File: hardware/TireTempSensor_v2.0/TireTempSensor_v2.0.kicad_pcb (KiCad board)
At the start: 4 copper layers, 27 x 53.8 mm, 54 parts, among them IC1 MAX15462AATA+, IC2 MLX90621ESF-BAB-000-SP, J1 SWD_01x06, J2 CAN_01x04, Q1 FQT3P20TF, SW1 RESET, U1 STM32L4P5RET6, U2 MIC5306-2.6YD5-TR, U3 SN65HVD232, Y1 16MGHz

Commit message: some pcb connections
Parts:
- F1: footprint Capacitor_SMD:C_1206_3216Metric -> Fuse:Fuse_1210_3225Metric
- J2: footprint Connector_PinHeader_1.27mm:PinHeader_1x04_P1.27mm_Vertical -> Connector_Wire:SolderWire-0.1sqmm_1x04_P3.6mm_D0.4mm_OD1mm_Relief
- moved FB1 19.8 mm to (119.8, 89.2)
- moved C14 8.33 mm to (124.5, 76.0), turned to -90 degrees
- moved C15 8.08 mm to (118.5, 75.2)
- moved U2 8.08 mm to (121.5, 75.0)
- moved FB2 7.41 mm to (122.8, 78.5), turned to 90 degrees
- moved J2 5.04 mm to (116.9, 115.5), turned to 180 degrees
- moved J1 4.86 mm to (123.5, 82.8)
- moved R6 3.00 mm to (116.8, 69.0)
- moved C17 3.00 mm to (108.8, 69.0)
- moved FB3 3.00 mm to (108.8, 72.2)
- moved R5 3.00 mm to (116.8, 72.2)
- moved IC2 2.95 mm to (114.5, 68.7)
- moved F1 2.69 mm to (114.0, 108.5)
- moved H1 2.00 mm to (122.2, 113.5)
- moved H2 2.00 mm to (103.2, 113.5)
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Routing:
- net GND: track 0.00 -> 15.6 mm
- net /+3V3_uC: track 0.00 -> 13.2 mm
- net +2V6: track 0.00 -> 12.9 mm
- net /OSC IN: track 0.00 -> 10.6 mm
- net Net-(F1-Pad2): track 0.00 -> 10.5 mm
- net Net-(R3-Pad1): track 0.00 -> 8.09 mm
- net /NRST: track 0.00 -> 8.01 mm
- net Net-(C14-Pad1): track 0.00 -> 6.32 mm
- net /CAN L: track 0.00 -> 4.41 mm
- net /CAN H: track 0.00 -> 4.41 mm
- net Net-(C17-Pad1): track 0.00 -> 4.24 mm
- net Net-(C10-Pad1): track 0.00 -> 3.98 mm
- net /Power Supply 3.3v 2.6v/+24V safe: track 0.00 -> 3.75 mm
- net Net-(FB4-Pad2): track 0.00 -> 2.85 mm
- net Net-(D6-Pad2): track 0.00 -> 2.61 mm
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- added copper zone on In1.Cu, net GND
- added copper zone on F.Cu, net Net-(L1-Pad1)
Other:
- board size 27 x 53.8 mm -> 27 x 54 mm

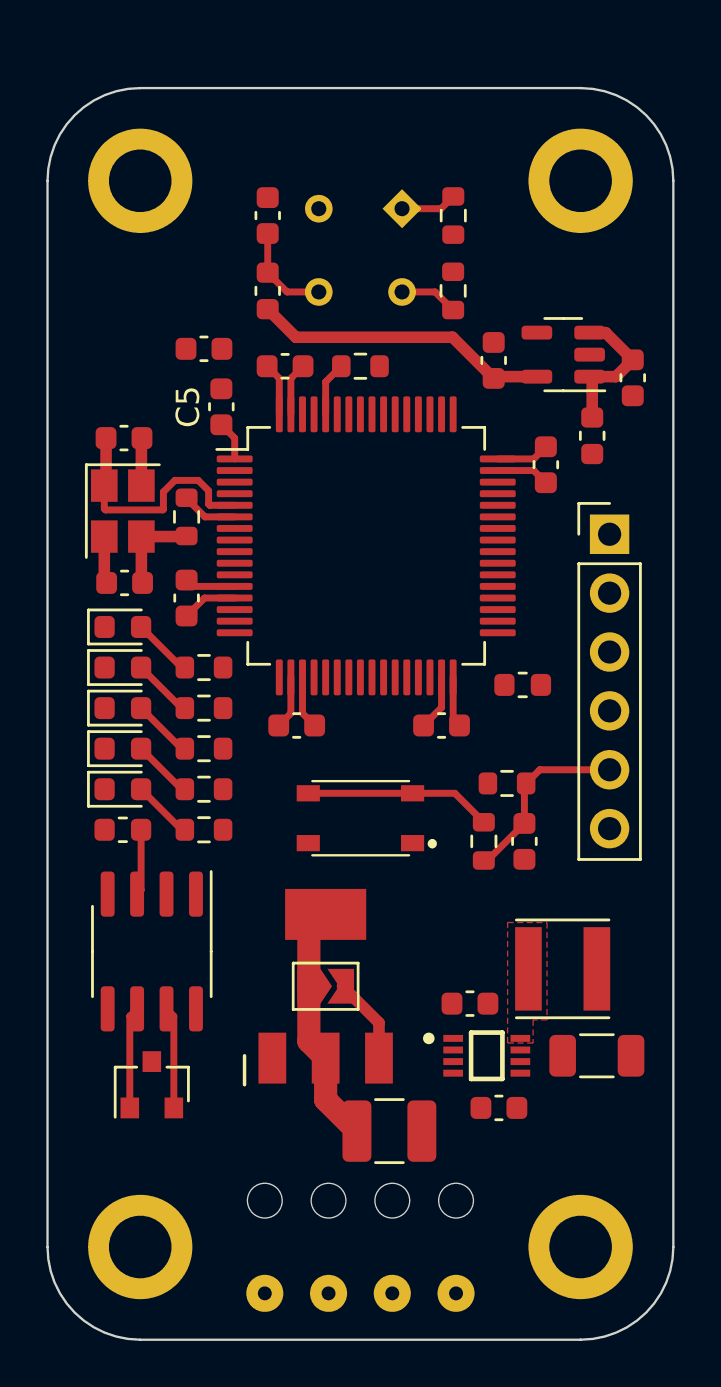
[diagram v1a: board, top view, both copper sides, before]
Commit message: more pcb connections
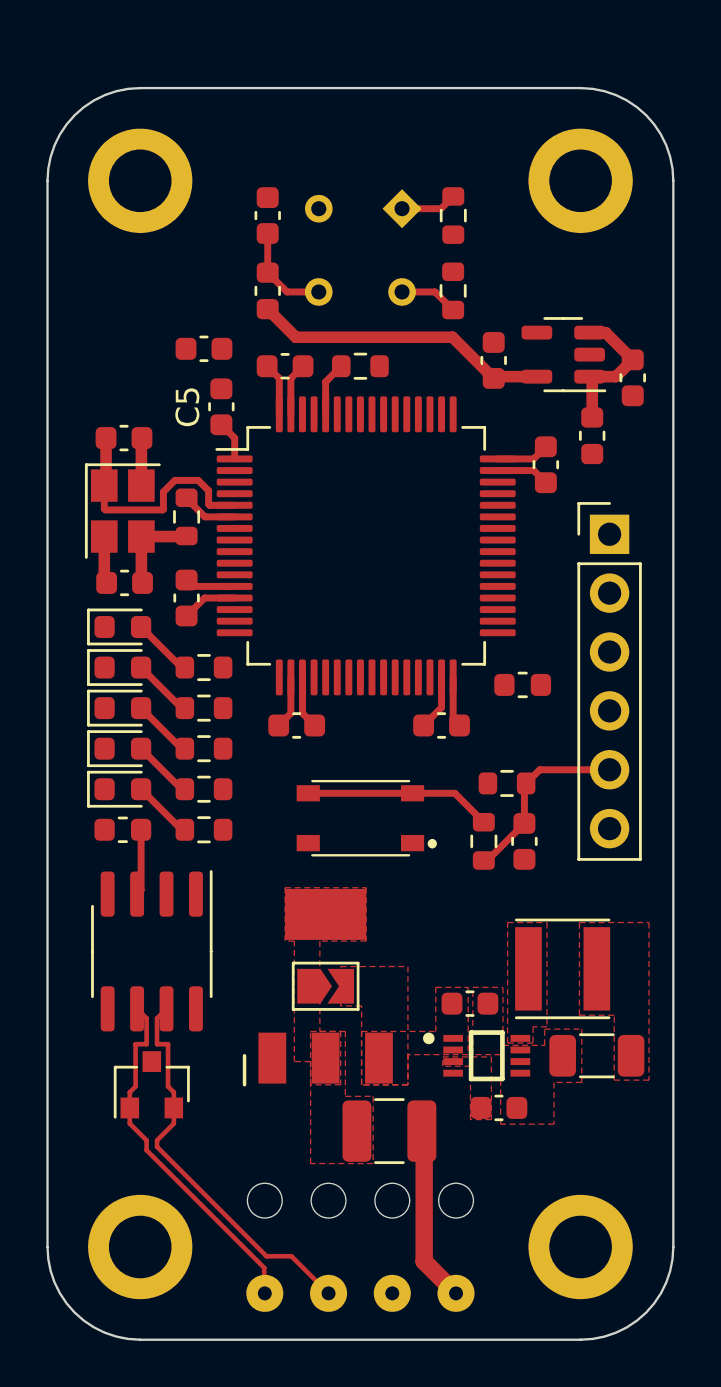
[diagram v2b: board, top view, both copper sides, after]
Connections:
- D1 pad 1: /CAN L -> /CAN -
- D1 pad 2: /CAN H -> /CAN +
- J2 pad 2: /CAN H -> GND
- J2 pad 3: /CAN L -> /CAN +
- J2 pad 4: GND -> /CAN -
- U3 pad 6: /CAN L -> /CAN -
- U3 pad 7: /CAN H -> /CAN +
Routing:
- net /CAN +: track 0.00 -> 17.0 mm
- net /CAN -: track 0.00 -> 15.4 mm
- net Net-(F1-Pad2): track 10.5 -> 0.00 mm
- net +24V: track 0.00 -> 7.61 mm
- net /CAN L: track 4.41 -> 0.00 mm
- net /CAN H: track 4.41 -> 0.00 mm
- net /Power Supply 3.3v 2.6v/+24V safe: track 3.75 -> 0.00 mm
- added copper zone on F.Cu, net +3V3
- added copper zone on F.Cu, net /Power Supply 3.3v 2.6v/+24V safe
- added copper zone on F.Cu, net GND
- added copper zone on F.Cu, net Net-(C13-Pad1)
- added copper zone on F.Cu, net Net-(F1-Pad2)

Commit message: gnd vias added
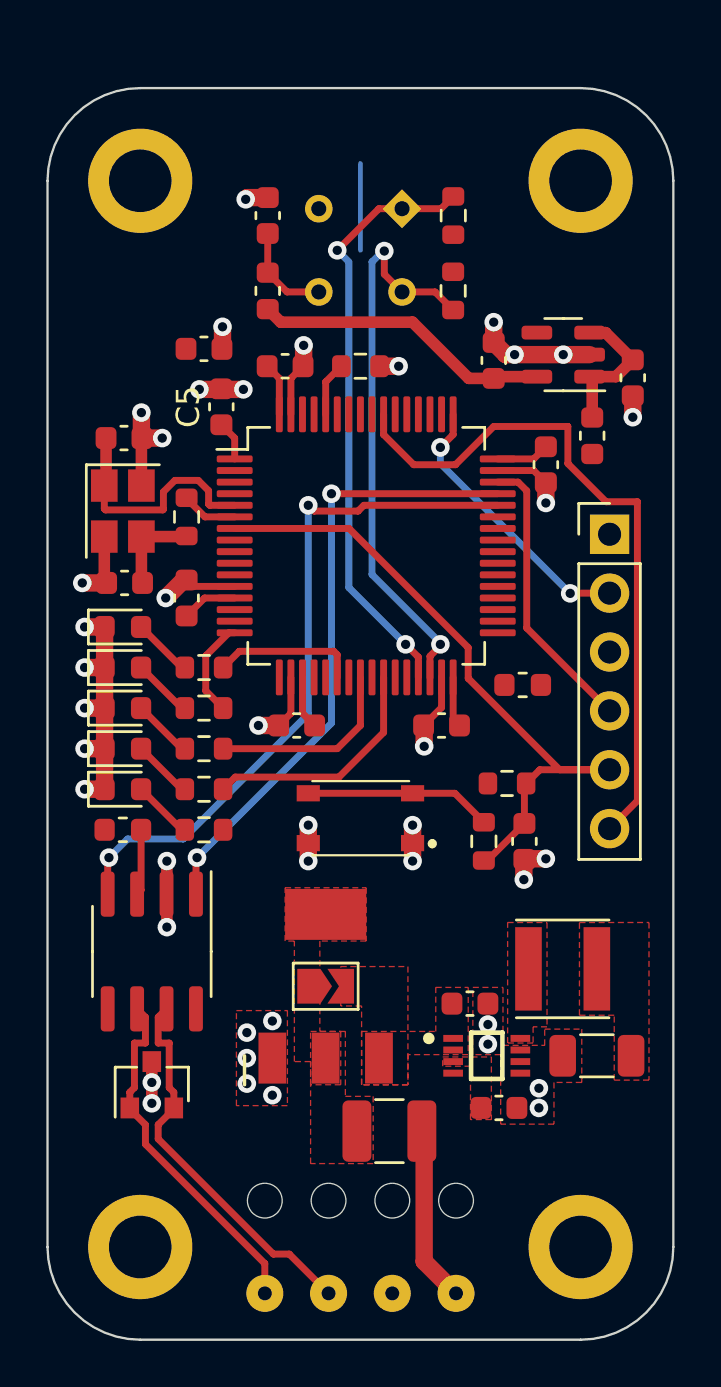
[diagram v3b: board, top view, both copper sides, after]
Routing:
- net GND: track 15.6 -> 55.1 mm, vias 0 -> 41
- net /CAN RX: track 0.00 -> 30.1 mm, vias 0 -> 2
- net /SWO: track 0.00 -> 29.9 mm
- net /CAN TX: track 0.00 -> 26.9 mm, vias 0 -> 2
- net /SCL: track 2.43 -> 25.8 mm, vias 0 -> 2
- net /SDA: track 2.53 -> 24.7 mm, vias 0 -> 2
- net /NRST: track 8.01 -> 29.3 mm
- net /SWDIO: track 0.00 -> 12.4 mm
- net /SWCLK: track 0.00 -> 12.0 mm, vias 0 -> 2
- net /LED OK: track 0.00 -> 10.3 mm
- net /LED WAR1: track 0.00 -> 8.41 mm
- net /LED ERR: track 0.00 -> 6.25 mm
- net /LED WAR2: track 0.00 -> 4.23 mm

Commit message: silkscreen text added
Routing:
- net +3V3: track 0.00 -> 9.09 mm, vias 0 -> 18
- net /+3V3_uC: track 13.2 -> 20.4 mm, vias 0 -> 8
- net GND: track 55.1 -> 54.2 mm, vias 41 -> 43
- net /CAN TX: track 26.9 -> 27.7 mm
- net /SWO: track 29.9 -> 30.5 mm
- added copper zone on In2.Cu, net +3V3
- added copper zone on In2.Cu, net /+3V3_uC
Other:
- board text added: "24V"
- board text added: "3V3"
- board text added: "CLK"
- board text added: "DIO"
- board text added: "GND"
- board text added: "H"
- board text added: "JLCJLCJLCJLC"
- board text added: "L"
- board text added: "NRST"
- board text added: "SWO"

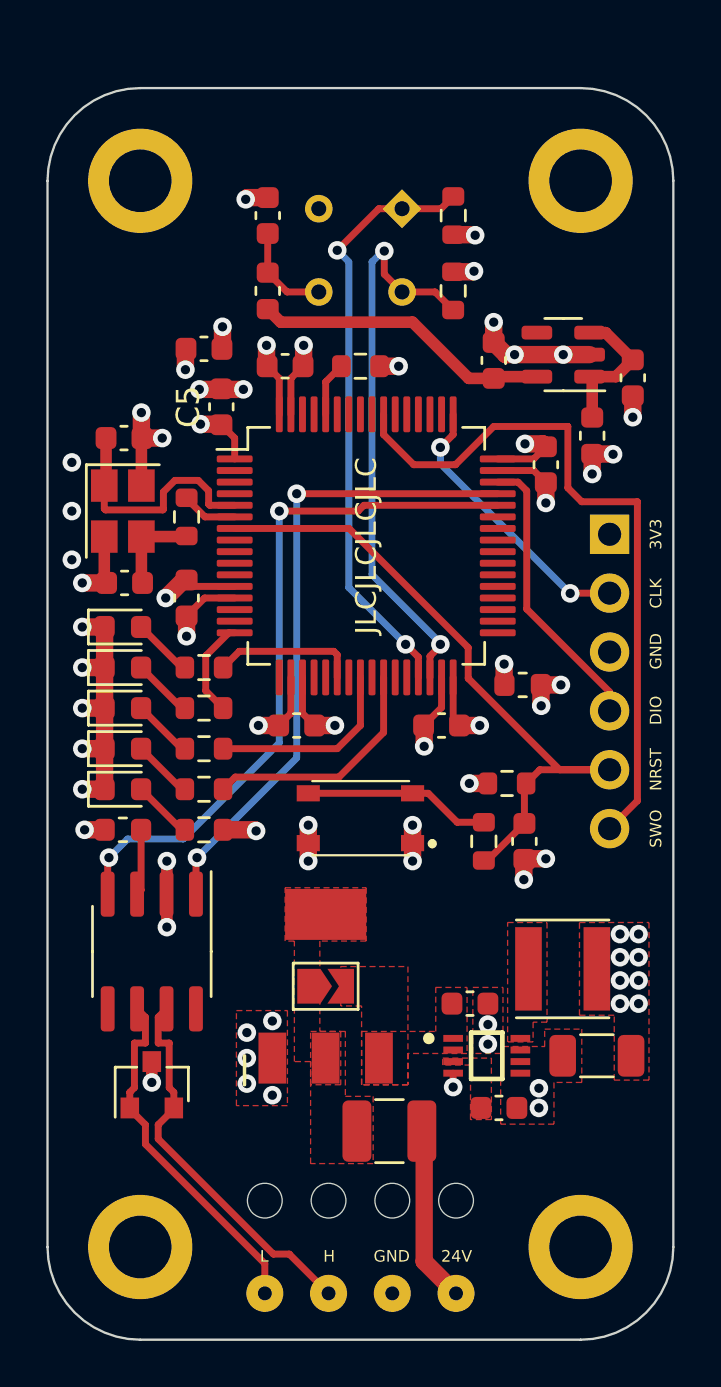
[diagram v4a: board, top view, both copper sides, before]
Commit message: front silkscreen
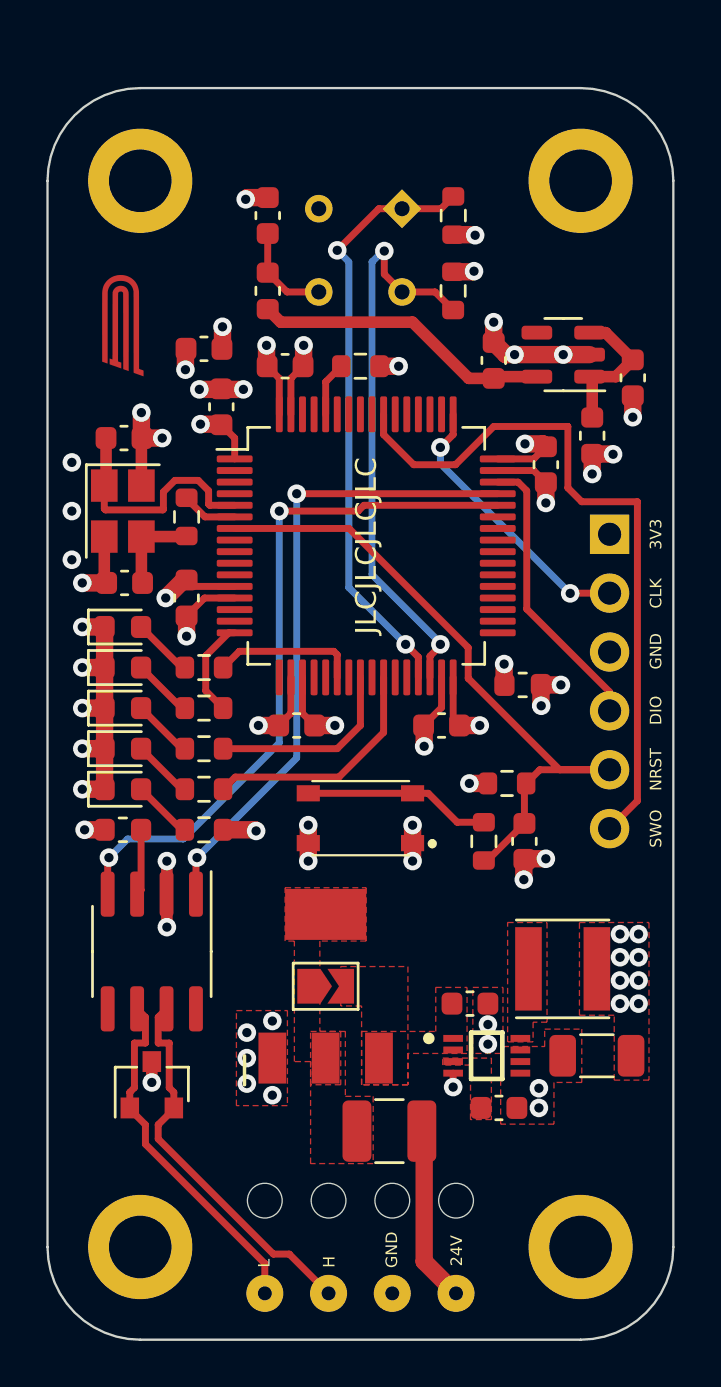
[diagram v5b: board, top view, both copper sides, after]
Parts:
- added G***: LOGO, logo:logo_3mm_FCu, F.Cu at (102.5, 73.8)
- added G***: LOGO, logo:logo_3mm_FMask, F.Cu at (102.5, 73.8)

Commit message: pcb is done
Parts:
- added G***: LOGO, mylogo:logo, B.Cu at (112.8, 90.5)
- J1: moved to B.Cu
- turned J1 to 180 degrees

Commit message: reviewed
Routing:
- net GND: track 54.2 -> 60.9 mm
- added copper zone on B.Cu, net GND
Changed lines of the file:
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@@
   (segment (start 107.7 76.5) (end 106.775 76.5) (width 0.75) (layer "F.Cu") (net 2))
   (segment (start 106.725 76.5) (end 106.75 76.475) (width 0.75) (layer "F.Cu") (net 2))
+  (segment (start 119.65 105) (end 121.225 105) (width 0.25) (layer "F.Cu") (net 2))
   (segment (start 110.3 74.6) (end 110.3 75.475) (width 0.75) (layer "F.Cu") (net 2))
+  (segment (start 121.225 105) (end 121.475 105.25) (width 0.25) (layer "F.Cu") (net 2))
   (segment (start 101.7125 90.25) (end 100.85 90.25) (width 0.75) (layer "F.Cu") (net 2))
   (segment (start 103.3 78.625) (end 103.325 78.6) (width 0.5) (layer "F.Cu") (net 2))
@@
   (segment (start 101.7125 92) (end 100.85 92) (width 0.75) (layer "F.Cu") (net 2))
   (segment (start 104.35 85.5) (end 105.125 84.725) (width 0.75) (layer "F.Cu") (net 2))
+  (segment (start 118.75 106.75) (end 118.75 105.25) (width 0.25) (layer "F.Cu") (net 2))
   (segment (start 105.8 76.5) (end 106.725 76.5) (width 0.75) (layer "F.Cu") (net 2))
   (segment (start 104.4 98.29) (end 104.385 98.275) (width 0.5) (layer "F.Cu") (net 2))
@@
   (segment (start 103.3 78.575) (end 103.325 78.6) (width 0.75) (layer "F.Cu") (net 2))
   (segment (start 105.125 84.725) (end 105.25 84.725) (width 0.75) (layer "F.Cu") (net 2))
+  (segment (start 118.75 105.25) (end 118.25 104.75) (width 0.25) (layer "F.Cu") (net 2))
   (segment (start 109.225 91) (end 109.75 90.475) (width 0.3) (layer "F.Cu") (net 2))
   (segment (start 124.5 77.7) (end 124.5 76.775) (width 0.75) (layer "F.Cu") (net 2))
@@
   (segment (start 110.5 95.3) (end 110.5 96.075) (width 0.75) (layer "F.Cu") (net 2))
   (segment (start 101.7125 88.5) (end 100.85 88.5) (width 0.75) (layer "F.Cu") (net 2))
+  (segment (start 119.5 107.5) (end 118.75 106.75) (width 0.25) (layer "F.Cu") (net 2))
   (segment (start 104.2 78.6) (end 103.325 78.6) (width 0.75) (layer "F.Cu") (net 2))
   (segment (start 101.7 82.85) (end 101.7 84.75) (width 0.5) (layer "F.Cu") (net 2))
@@
   (segment (start 104.4 98.26) (end 104.385 98.275) (width 0.5) (layer "F.Cu") (net 2))
   (segment (start 103.3 80.65) (end 103.3 78.625) (width 0.5) (layer "F.Cu") (net 2))
+  (segment (start 118.5 105) (end 119.65 105) (width 0.25) (layer "F.Cu") (net 2))
   (segment (start 103.75 105.5) (end 103.75 106.4) (width 0.5) (layer "F.Cu") (net 2))
   (segment (start 121.5 75) (end 122.6375 75) (width 0.75) (layer "F.Cu") (net 2))
@@
   (segment (start 110.5 96.85) (end 110.5 96.075) (width 0.75) (layer "F.Cu") (net 2))
   (segment (start 115.5 91.9) (end 115.5 91.025) (width 0.75) (layer "F.Cu") (net 2))
+  (segment (start 118.25 104.75) (end 118.5 105) (width 0.25) (layer "F.Cu") (net 2))
   (segment (start 119.85 96.75) (end 119.825 96.775) (width 0.75) (layer "F.Cu") (net 2))
   (segment (start 105.525 85) (end 107.325 85) (width 0.3) (layer "F.Cu") (net 2))
@@
   )
   (zone (net 6) (net_name "/Power Supply 3.3v 2.6v/+24V safe") (layer "F.Cu") (hatch full 0.508)
+    (priority 1)
     (connect_pads yes (clearance 0))
     (min_thickness 0.254) (filled_areas_thickness no)
@@
   )
   (zone (net 29) (net_name "Net-(IC1-Pad8)") (layer "F.Cu") (hatch edge 0.508)
+    (priority 1)
     (connect_pads yes (clearance 0))
     (min_thickness 0.254) (filled_areas_thickness no)
@@
   )
   (zone (net 10) (net_name "+3V3") (layer "F.Cu") (hatch full 0.508)
+    (priority 1)
     (connect_pads yes (clearance 0))
     (min_thickness 0.254) (filled_areas_thickness no)
@@
   )
   (zone (net 7) (net_name "Net-(C13-Pad1)") (layer "F.Cu") (hatch full 0.508)
-    (connect_pads yes (clearance 0))
+    (priority 1)
+    (connect_pads yes (clearance 0.2))
     (min_thickness 0.254) (filled_areas_thickness no)
     (fill yes (thermal_gap 0) (thermal_bridge_width 0.3))
@@
     )
   )
-  (zone (net 2) (net_name "GND") (layer "F.Cu") (hatch full 0.508)
-    (connect_pads yes (clearance 0))
-    (min_thickness 0.254) (filled_areas_thickness no)
-    (fill yes (thermal_gap 0) (thermal_bridge_width 0.3))
-    (polygon
-      (pts
-        (xy 118.9 104.85)
-        (xy 120.7 104.85)
-        (xy 120.7 104.1)
-        (xy 122.3 104.1)
-        (xy 122.3 106.4)
-        (xy 121.1 106.4)
-        (xy 121.1 108.2)
-        (xy 118.8 108.2)
-        (xy 118.8 105.15)
-        (xy 117.6 105.15)
-        (xy 117.6 102.3)
-        (xy 118.9 102.3)
+  (zone (net 2) (net_name "GND") (layers "F.Cu" "In1.Cu" "B.Cu") (hatch edge 0.508)
+    (connect_pads (clearance 0.508))
+    (min_thickness 0.254) (filled_areas_thickness no)
+    (fill yes (thermal_gap 0.508) (thermal_bridge_width 0.508))
+    (polygon
+      (pts
+        (xy 126.25 117.5)
+        (xy 99.25 117.5)
+        (xy 99.25 63.5)
+        (xy 126.25 63.5)
       )
     )
   )
   (zone (net 18) (net_name "Net-(F1-Pad2)") (layer "F.Cu") (hatch full 0.508)
+    (priority 1)
     (connect_pads yes (clearance 0))
     (min_thickness 0.254) (filled_areas_thickness no)
@@
   )
   (zone (net 18) (net_name "Net-(F1-Pad2)") (layer "F.Cu") (hatch full 0.508)
+    (priority 1)
     (connect_pads yes (clearance 0))
     (min_thickness 0.254) (filled_areas_thickness no)
@@
   )
   (zone (net 6) (net_name "/Power Supply 3.3v 2.6v/+24V safe") (layer "F.Cu") (hatch full 0.508)
+    (priority 1)
     (connect_pads yes (clearance 0))
     (min_thickness 0.254) (filled_areas_thickness no)
@@
         (xy 111.9 101.4)
         (xy 114.8 101.4)
-      )
-    )
-  )
-  (zone (net 2) (net_name "GND") (layer "In1.Cu") (hatch edge 0.508)
-    (connect_pads (clearance 0.508))
-    (min_thickness 0.254) (filled_areas_thickness no)
-    (fill yes (thermal_gap 0.508) (thermal_bridge_width 0.508))
-    (polygon
-      (pts
-        (xy 127.5 120)
-        (xy 97.5 120)
-        (xy 97.5 62.5)
-        (xy 127.5 62.5)
       )
     )
@@
   )
   (zone (net 10) (net_name "+3V3") (layer "In2.Cu") (hatch edge 0.508)
+    (priority 1)
     (connect_pads yes (clearance 0))
     (min_thickness 0.254) (filled_areas_thickness no)
@@
   )
   (zone (net 1) (net_name "/+3V3_uC") (layer "In2.Cu") (hatch edge 0.508)
-    (connect_pads yes (clearance 0))
+    (connect_pads yes (clearance 0.45))
     (min_thickness 0.254) (filled_areas_thickness no)
     (fill yes (thermal_gap 0.508) (thermal_bridge_width 0.508))
@@
   )
   (zone (net 10) (net_name "+3V3") (layer "In2.Cu") (hatch edge 0.508)
-    (connect_pads yes (clearance 0))
-    (min_thickness 0.254) (filled_areas_thickness no)
+    (priority 1)
+    (connect_pads yes (clearance 0))
+    (min_thickness 0.254) (filled_areas_thickness no)
